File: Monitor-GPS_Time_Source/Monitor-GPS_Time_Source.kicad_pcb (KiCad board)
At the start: 2 copper layers, 21.4 x 26.5 mm, 17 parts, among them J1 2x5, 1.27mm, J2 1x10, 2.54mm, J3 1x10, 2.54mm, J4 1x3, 2.54mm, SW2 ALPS SKRK, U1 MSPM0C1105, U2 BL8565

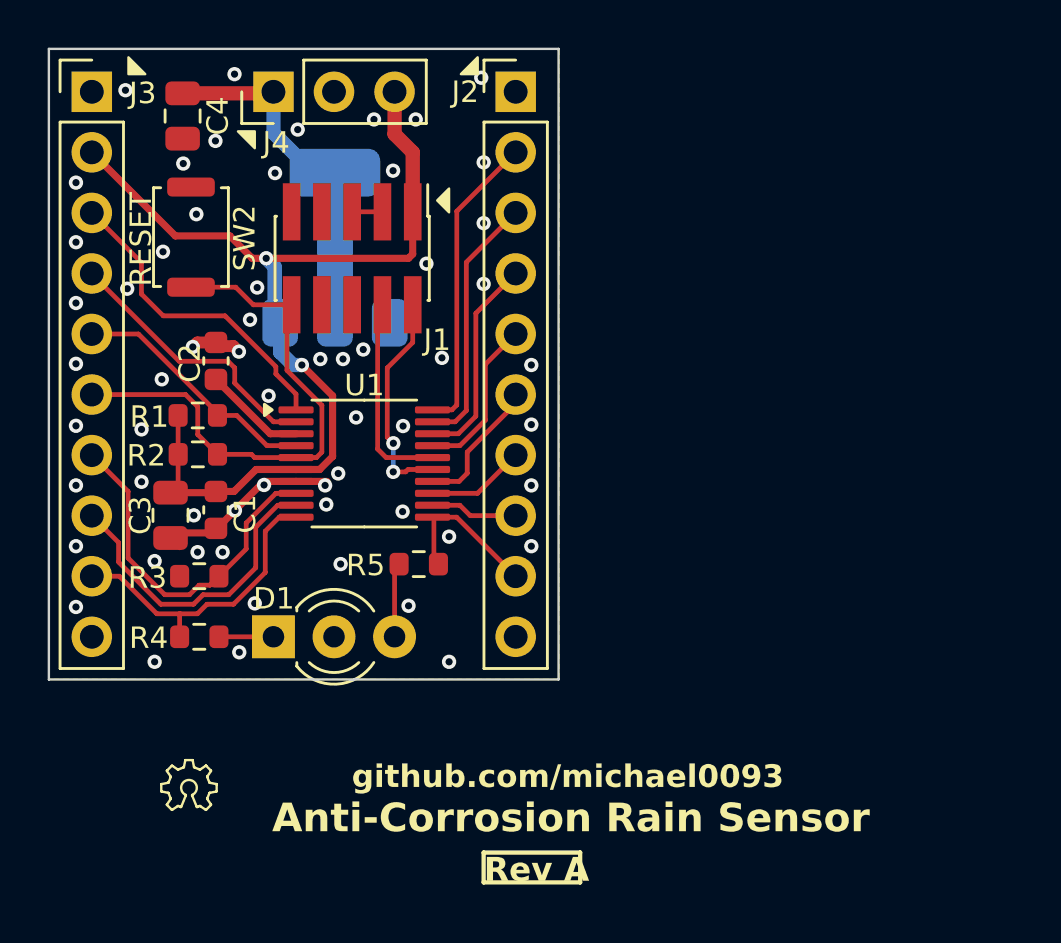
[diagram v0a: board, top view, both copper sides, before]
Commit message: Update code to match PCB rev A (was EVB). Minor sch corrections
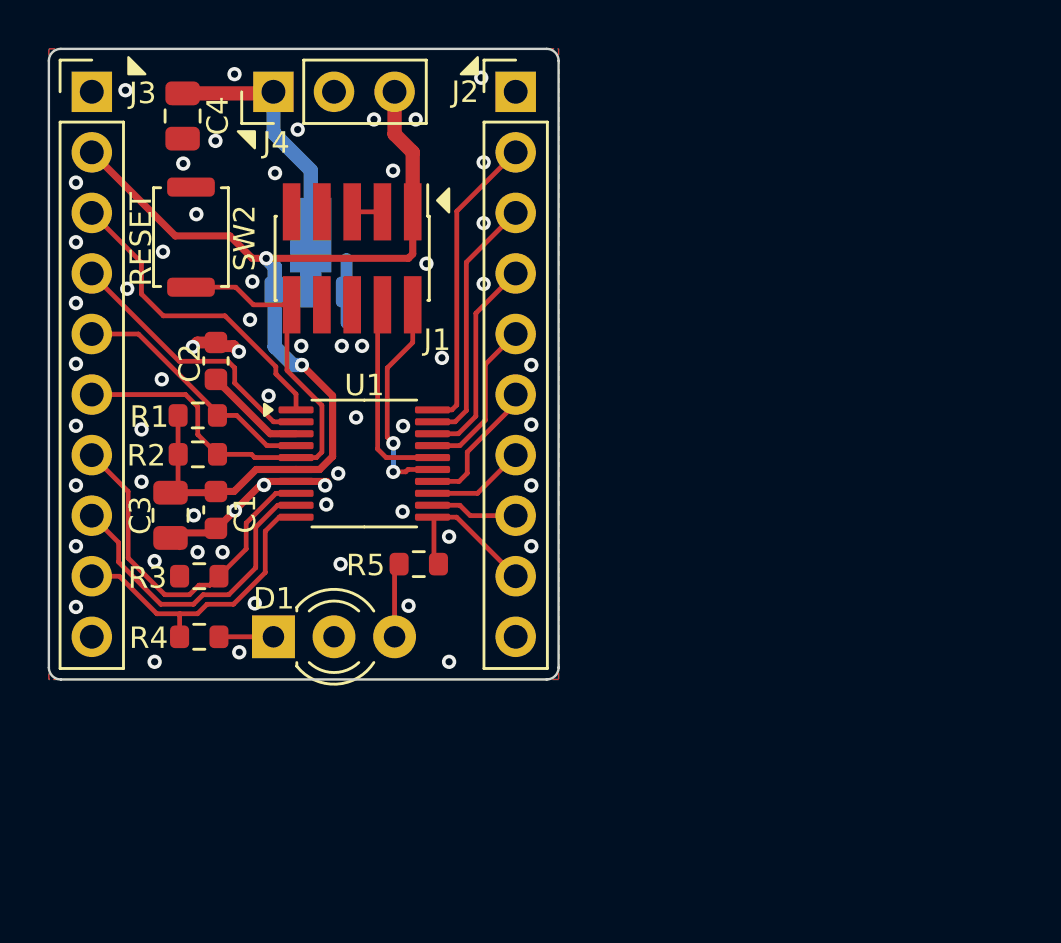
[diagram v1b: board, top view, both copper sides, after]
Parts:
- J1: value 2x5, 1.27mm -> Conn_ARM_JTAG_SWD_10
- J2, J3: value 1x10, 2.54mm -> Conn_01x10_Pin
- J4: value 1x3, 2.54mm -> Conn_01x03_Pin
- SW2: value ALPS SKRK -> SW_Push
- U2: value BL8565 -> BL8565CC3BTR33; footprint Package_TO_SOT_SMD:SOT-223-3_TabPin2 -> Package_TO_SOT_SMD:SOT-89-3
- moved U2 1.02 mm to (152.9, 82.9)
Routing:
- net GND: track 11.6 -> 14.3 mm
- net VIN: track 15.1 -> 12.8 mm
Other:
- outline, holes or cut-outs redrawn
- board text added: "github.com/ michael0093"
- board text removed: "Anti-Corrosion Rain Sensor"
- board text removed: "github.com/michael0093"
